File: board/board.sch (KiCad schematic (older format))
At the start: 41 parts, among them J1 USB_B_Micro, J4 SWD_CONN, J5 JTAG_CONN, J6 UART_Conn, J7 SPI_CONN, J8 I2C_CONN, SW3 SW_DPDT_x2, U5 SN74LVC8T245, U6 SN74LVC8T245

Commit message: Update for release.
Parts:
- C18, C19, C20, C21: Comment (none) -> Substitution Okay; Digikey (none) -> 1276-1857-1-ND
- D1: Comment (none) -> Substitution Okay; Digikey (none) -> 732-4979-1-ND; P/N (none) -> 150060SS75000
- D2, D3, D4: Comment (none) -> Substitution Okay; Digikey (none) -> 732-4979-1-ND; P/N 19-213-R6C-AP1Q2B-3T -> 150060SS75000
- D5, D6: Digikey (none) -> RB751S40T1GOSCT-ND; P/N RB751S40 -> RB751S40T1G
- FB3: Digikey (none) -> 445-1567-1-ND
- J1: Digikey (none) -> 609-4050-1-ND
- J4: Digikey (none) -> 609-6118-1-ND
- J5: Digikey (none) -> 609-6477-1-ND; P/N (none) -> 95278-801A20LF
- J6: Digikey (none) -> TSM-109-01-L-SV-P-ND; P/N TSM-109-01-L-SV -> TSM-109-01-L-SV-P
- J7, J8: Digikey (none) -> 609-5811-1-ND; P/N (none) -> 95278-101A08LF
- R10, R8, R9: Comment (none) -> Substitution Okay; Digikey (none) -> RMCF0603JT1K00CT-ND
- R11, R12, R13: Comment (none) -> Substitution Okay; Digikey (none) -> RMCF0603JT10K0CT-ND
- R14: Comment (none) -> Substitution Okay; Digikey (none) -> RMCF0603JT1M00CT-ND
- R15: Comment (none) -> Substitution Okay; Digikey (none) -> RMCF0603JT1K00CT-ND; P/N (none) -> RMCF0603JT1K00
- R16, R17: Comment (none) -> Substitution Okay; Digikey (none) -> RMCF0603JT2K20CT-ND
- R21, R22: Comment (none) -> Substitution Okay; Digikey (none) -> RMCF0603JT10K0CT-ND; P/N (none) -> RMCF0603JT10K0
- R7: Comment (none) -> Substitution Okay; Digikey (none) -> RMCF0603JT330RCT-ND; P/N (none) -> RMCF0603JT330R
- RN1, RN4: Digikey (none) -> Y1104CT-ND
- RN2, RN3: Digikey (none) -> Y1331CT-ND
- SW3: Digikey (none) -> 401-2002-1-ND; P/N (none) -> JS202011SCQN
- U5, U6: Digikey (none) -> 296-21065-1-ND

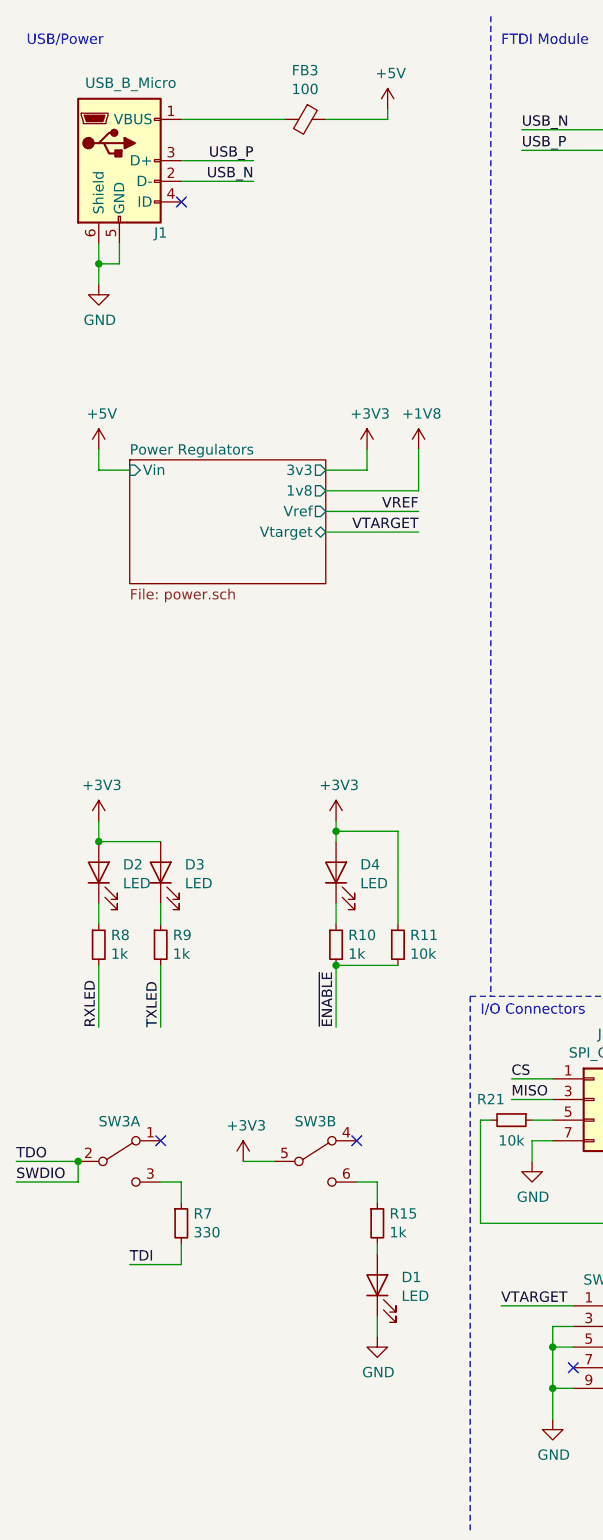
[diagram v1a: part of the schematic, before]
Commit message: Add protection (ESD, PTC fusing) to MicroUSB port
Schematic changes:

* No connect SHIELD on the MicroUSB port. Since we have no SHIELD GND, I
think it's best to leave the shield unconnected rather than connect it
to our digital GND and potentially introduce noise. This seems to be
backed up by the FTDI USB Design Guidelines
(https://www.ftdichip.com/Support/Documents/AppNotes/AN_146_USB_Hardware_Design_Guidelines_for_FTDI_ICs.pdf)
* Inline a USBLC-6 for transient voltage supression on our USB data lines
and VBUS
* Add a 500mA hold current PTC after the ferrite bead on VBUS. This PTC
should help protect the host computer if the board short circuits

Layout changes:

* Moves the passives (C2, C1, FB1, R1, FB2, C4, C5, R2) around the
MicroUSB port slightly outward to make room for the USBLC-6
* Place USBLC-6 close to the MicroUSB port
* Place PTC next to FB3

Component Selection:

* USBLC-6 is a popular choice for USB transient voltage supression. It's
very low capacitance so it shouldn't have an impact on data
integrity/speed. The SOT-666 package is common and compact, but still
easy enough to place by hand. It's also cheap at just $0.32 (100x)
* The Littelfuse NanoSMD fuse is rated for 13.2V and a 500mA hold
current. It trips at 1.1A with a fast 100ms time to trip. The 1206
footprint is compact and it's easy to place by hand. It's pretty cheap
at $0.32 (100x)
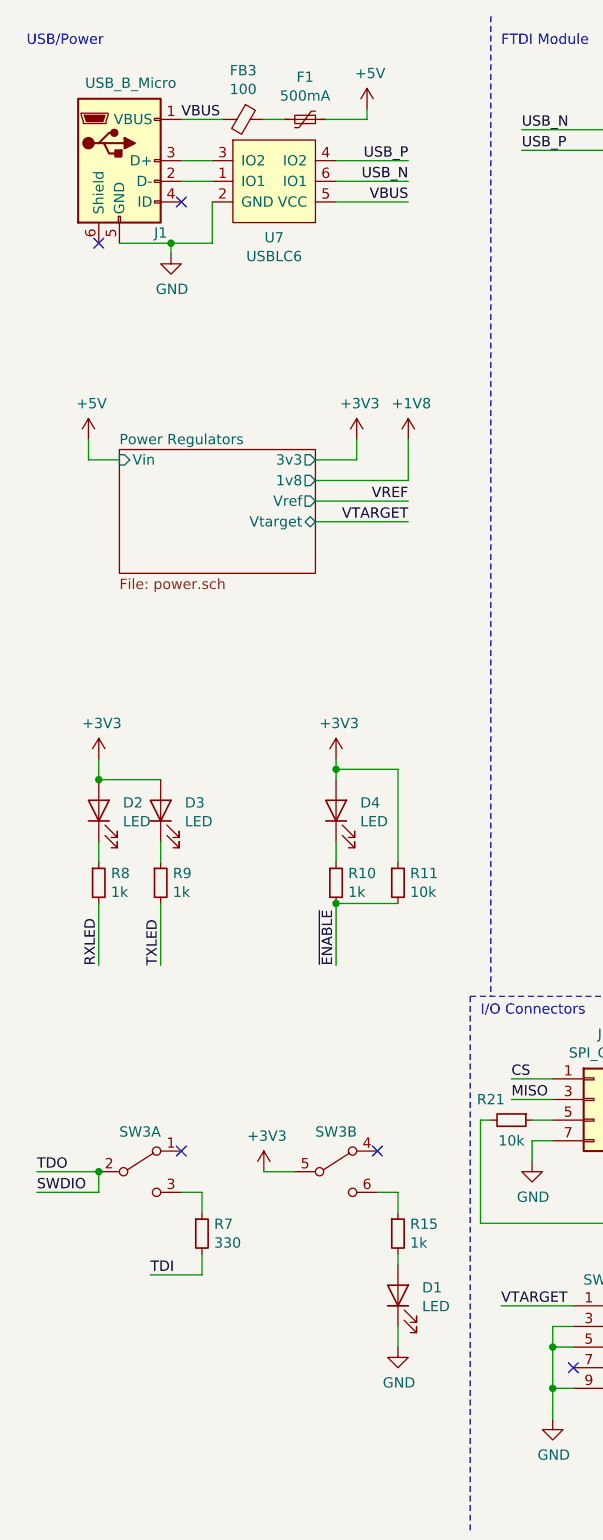
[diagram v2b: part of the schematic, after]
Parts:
- added F1: 500mA, Fuse:Fuse_1206_3216Metric, symbol Device:Polyfuse_Small
- added U7: USBLC6, Package_TO_SOT_SMD:SOT-666, symbol board-rescue:USBLC6
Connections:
- net +5V: now also F1.1; no longer FB3.1
- net GND: now also U7.2 (GND); no longer J1.6 (Shield)
- net USB_N: now also U7.6 (IO1); no longer J1.2 (D-)
- net USB_P: now also U7.4 (IO2); no longer J1.3 (D+)
- net VBUS: now reaches FB3.2, J1.1 (VBUS)
- net VBUS: now also U7.5 (VCC)
- new net: J1.2 (D-), U7.1 (IO1)
- new net: J1.3 (D+), U7.3 (IO2)
- new net: F1.2, FB3.1
- no-connect marks 33 -> 34
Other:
- moved on the sheet: D1, D2, D3, D4, FB3, R10, R11, R15, R7, R8, R9, SW3A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
